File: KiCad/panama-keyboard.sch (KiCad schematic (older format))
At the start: 170 parts, among them J1 MX, J2 USB_C_Receptacle_USB2.0, J3 AVR-ISP-6, K1 MX, M1 MX, P1 MX, Q1 MX, T1 MX, U1 MX, U2 ATmega32A-PU, X1 MX, Y1 MX, Y2 Crystal

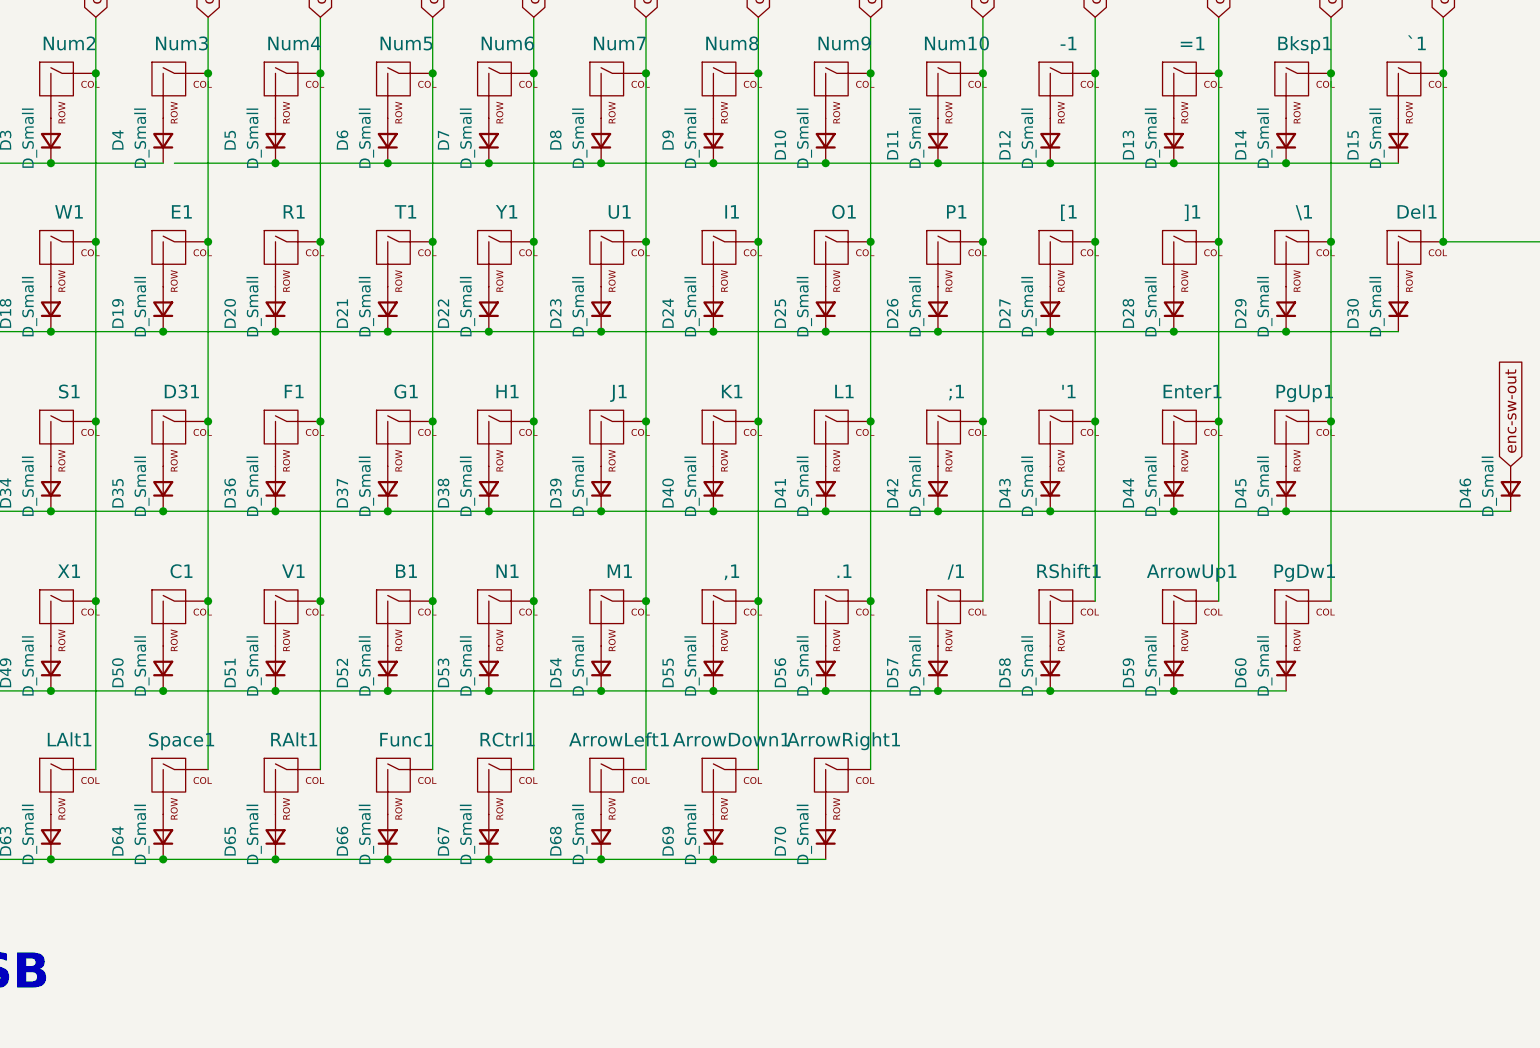
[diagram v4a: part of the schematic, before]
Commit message: pcb progress, moved switch matrix
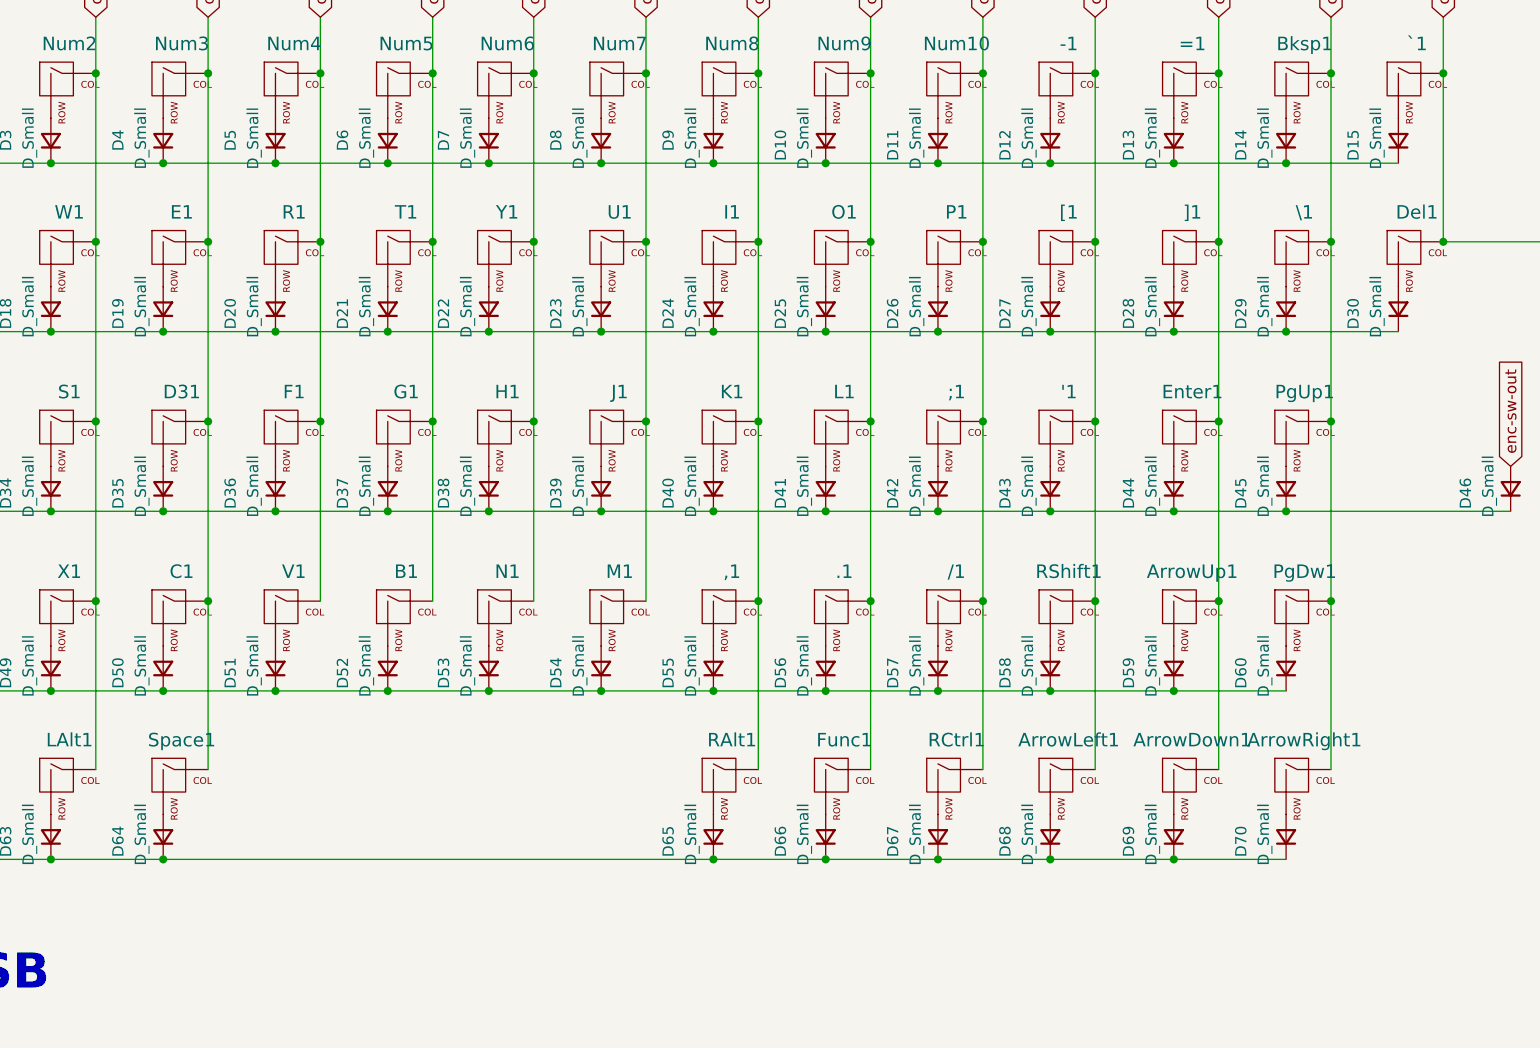
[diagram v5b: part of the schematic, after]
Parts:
- J3: footprint Connector_PinHeader_2.54mm:PinHeader_2x03_P2.54mm_Vertical -> Connector_PinHeader_2.54mm:PinHeader_1x06_P2.54mm_Horizontal
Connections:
- net col10: now also RCtrl1.1 (COL)
- net col11: now also ArrowLeft1.1 (COL)
- net col12: now also ArrowDown1.1 (COL)
- net col13: now also ArrowRight1.1 (COL)
- net col4: no longer RAlt1.1 (COL)
- net col5: no longer Func1.1 (COL)
- net col6: no longer RCtrl1.1 (COL)
- net col7: no longer ArrowLeft1.1 (COL)
- net col8: now also RAlt1.1 (COL); no longer ArrowDown1.1 (COL)
- net col9: now also Func1.1 (COL); no longer ArrowRight1.1 (COL)
- net row0: now also D10.1 (K), D11.1 (K), D12.1 (K), D13.1 (K), D14.1 (K), D15.1 (K), D5.1 (K), D6.1 (K), D7.1 (K), D8.1 (K), D9.1 (K)
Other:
- moved on the sheet: ArrowDown1, ArrowLeft1, ArrowRight1, D65, D66, D67, D68, D69, D70, Func1, RAlt1, RCtrl1
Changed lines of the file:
@@
 L Keyboard:MX RAlt1
 U 1 1 5F1DF75E
-P 6850 4600
-F 0 "RAlt1" H 6883 4781 60  0000 C CNN
-F 1 "MX" H 6825 4650 20  0001 C CNN
-F 2 "Button_Switch_Keyboard:SW_Cherry_MX_1.00u_PCB" H 6225 4575 60  0001 C CNN
-F 3 "" H 6225 4575 60  0001 C CNN
-	1    6850 4600
+P 8800 4600
+F 0 "RAlt1" H 8833 4781 60  0000 C CNN
+F 1 "MX" H 8775 4650 20  0001 C CNN
+F 2 "Button_Switch_Keyboard:SW_Cherry_MX_1.00u_PCB" H 8175 4575 60  0001 C CNN
+F 3 "" H 8175 4575 60  0001 C CNN
+	1    8800 4600
 	1    0    0    -1
 $EndComp
@@
 L Device:D_Small D65
 U 1 1 5F1DF76A
-P 6800 4850
-F 0 "D65" H 6850 5050 50  0000 R CNN
-F 1 "D_Small" H 6950 4950 50  0000 R CNN
-F 2 "Diode_THT:D_DO-35_SOD27_P7.62mm_Horizontal" V 6800 4850 50  0001 C CNN
-F 3 "~" V 6800 4850 50  0001 C CNN
-	1    6800 4850
-	0    -1   -1   0
-$EndComp
-$Comp
-L Keyboard:MX Func1
-U 1 1 5F1DF770
-P 7350 4600
-F 0 "Func1" H 7383 4781 60  0000 C CNN
-F 1 "MX" H 7325 4650 20  0001 C CNN
-F 2 "Button_Switch_Keyboard:SW_Cherry_MX_1.00u_PCB" H 6725 4575 60  0001 C CNN
-F 3 "" H 6725 4575 60  0001 C CNN
-	1    7350 4600
-	1    0    0    -1
-$EndComp
-$Comp
-L Device:D_Small D66
-U 1 1 5F1DF776
-P 7300 4850
-F 0 "D66" H 7350 5050 50  0000 R CNN
-F 1 "D_Small" H 7450 4950 50  0000 R CNN
-F 2 "Diode_THT:D_DO-35_SOD27_P7.62mm_Horizontal" V 7300 4850 50  0001 C CNN
-F 3 "~" V 7300 4850 50  0001 C CNN
-	1    7300 4850
-	0    -1   -1   0
-$EndComp
-$Comp
-L Keyboard:MX ArrowLeft1
-U 1 1 5F1DF77C
-P 8300 4600
-F 0 "ArrowLeft1" H 8333 4781 60  0000 C CNN
-F 1 "MX" H 8275 4650 20  0001 C CNN
-F 2 "Button_Switch_Keyboard:SW_Cherry_MX_1.00u_PCB" H 7675 4575 60  0001 C CNN
-F 3 "" H 7675 4575 60  0001 C CNN
-	1    8300 4600
-	1    0    0    -1
-$EndComp
-$Comp
-L Keyboard:MX ArrowDown1
-U 1 1 5F1DF782
-P 8800 4600
-F 0 "ArrowDown1" H 8833 4781 60  0000 C CNN
-F 1 "MX" H 8775 4650 20  0001 C CNN
-F 2 "Button_Switch_Keyboard:SW_Cherry_MX_1.00u_PCB" H 8175 4575 60  0001 C CNN
-F 3 "" H 8175 4575 60  0001 C CNN
-	1    8800 4600
-	1    0    0    -1
-$EndComp
-$Comp
-L Device:D_Small D68
-U 1 1 5F1DF788
-P 8250 4850
-F 0 "D68" H 8300 5050 50  0000 R CNN
-F 1 "D_Small" H 8400 4950 50  0000 R CNN
-F 2 "Diode_THT:D_DO-35_SOD27_P7.62mm_Horizontal" V 8250 4850 50  0001 C CNN
-F 3 "~" V 8250 4850 50  0001 C CNN
-	1    8250 4850
-	0    -1   -1   0
-$EndComp
-$Comp
-L Device:D_Small D69
-U 1 1 5F1DF78E
 P 8750 4850
-F 0 "D69" H 8800 5050 50  0000 R CNN
+F 0 "D65" H 8800 5050 50  0000 R CNN
 F 1 "D_Small" H 8900 4950 50  0000 R CNN
 F 2 "Diode_THT:D_DO-35_SOD27_P7.62mm_Horizontal" V 8750 4850 50  0001 C CNN
@@
 $EndComp
 $Comp
-L Keyboard:MX ArrowRight1
-U 1 1 5F1DF794
+L Keyboard:MX Func1
+U 1 1 5F1DF770
 P 9300 4600
-F 0 "ArrowRight1" H 9333 4781 60  0000 C CNN
+F 0 "Func1" H 9333 4781 60  0000 C CNN
 F 1 "MX" H 9275 4650 20  0001 C CNN
 F 2 "Button_Switch_Keyboard:SW_Cherry_MX_1.00u_PCB" H 8675 4575 60  0001 C CNN
@@
 $EndComp
 $Comp
-L Device:D_Small D70
-U 1 1 5F1DF79A
+L Device:D_Small D66
+U 1 1 5F1DF776
 P 9250 4850
-F 0 "D70" H 9300 5050 50  0000 R CNN
+F 0 "D66" H 9300 5050 50  0000 R CNN
 F 1 "D_Small" H 9400 4950 50  0000 R CNN
 F 2 "Diode_THT:D_DO-35_SOD27_P7.62mm_Horizontal" V 9250 4850 50  0001 C CNN
 F 3 "~" V 9250 4850 50  0001 C CNN
 	1    9250 4850
+	0    -1   -1   0
+$EndComp
+$Comp
+L Keyboard:MX ArrowLeft1
+U 1 1 5F1DF77C
+P 10300 4600
+F 0 "ArrowLeft1" H 10333 4781 60  0000 C CNN
+F 1 "MX" H 10275 4650 20  0001 C CNN
+F 2 "Button_Switch_Keyboard:SW_Cherry_MX_1.00u_PCB" H 9675 4575 60  0001 C CNN
+F 3 "" H 9675 4575 60  0001 C CNN
+	1    10300 4600
+	1    0    0    -1
+$EndComp
+$Comp
+L Keyboard:MX ArrowDown1
+U 1 1 5F1DF782
+P 10850 4600
+F 0 "ArrowDown1" H 10883 4781 60  0000 C CNN
+F 1 "MX" H 10825 4650 20  0001 C CNN
+F 2 "Button_Switch_Keyboard:SW_Cherry_MX_1.00u_PCB" H 10225 4575 60  0001 C CNN
+F 3 "" H 10225 4575 60  0001 C CNN
+	1    10850 4600
+	1    0    0    -1
+$EndComp
+$Comp
+L Device:D_Small D68
+U 1 1 5F1DF788
+P 10250 4850
+F 0 "D68" H 10300 5050 50  0000 R CNN
+F 1 "D_Small" H 10400 4950 50  0000 R CNN
+F 2 "Diode_THT:D_DO-35_SOD27_P7.62mm_Horizontal" V 10250 4850 50  0001 C CNN
+F 3 "~" V 10250 4850 50  0001 C CNN
+	1    10250 4850
+	0    -1   -1   0
+$EndComp
+$Comp
+L Device:D_Small D69
+U 1 1 5F1DF78E
+P 10800 4850
+F 0 "D69" H 10850 5050 50  0000 R CNN
+F 1 "D_Small" H 10950 4950 50  0000 R CNN
+F 2 "Diode_THT:D_DO-35_SOD27_P7.62mm_Horizontal" V 10800 4850 50  0001 C CNN
+F 3 "~" V 10800 4850 50  0001 C CNN
+	1    10800 4850
 	0    -1   -1   0
 $EndComp
@@
 	5800 1850 6300 1850
 Connection ~ 5800 1850
-Wire Wire Line
-	6350 1850 6800 1850
 Connection ~ 6800 1850
 Wire Wire Line
@@
 Wire Wire Line
 	5800 4950 6300 4950
-Connection ~ 6300 4950
-Wire Wire Line
-	6300 4950 6800 4950
-Connection ~ 6800 4950
-Connection ~ 8250 4950
-Wire Wire Line
-	8250 4950 8750 4950
 Connection ~ 8750 4950
-Wire Wire Line
-	8750 4950 9250 4950
 Wire Wire Line
 	5500 1200 5500 1450
@@
 Wire Wire Line
 	7000 3000 7000 3800
-Connection ~ 7000 3800
-Wire Wire Line
-	7000 3800 7000 4550
+Wire Wire Line
+	8950 3800 8950 4550
 Wire Wire Line
 	7500 1200 7500 1450
@@
 Wire Wire Line
 	7500 3000 7500 3800
-Connection ~ 7500 3800
-Wire Wire Line
-	7500 3800 7500 4550
+Wire Wire Line
+	9450 3800 9450 4550
 Wire Wire Line
 	7950 1200 7950 1450
@@
 	7950 3000 7950 3800
 Wire Wire Line
-	8450 3800 8450 4550
+	10450 3800 10450 4550
 Wire Wire Line
 	8450 1200 8450 1450
@@
 Wire Wire Line
 	8450 3000 8450 3800
-Connection ~ 8450 3800
-Wire Wire Line
-	8950 3800 8950 4550
+Wire Wire Line
+	11000 3800 11000 4550
 Wire Wire Line
 	8950 1200 8950 1450
@@
 Wire Wire Line
 	8950 3000 8950 3800
-Connection ~ 8950 3800
-Wire Wire Line
-	9450 3800 9450 4550
 Wire Wire Line
 	9450 1200 9450 1450
@@
 F 0 "J3" H 4771 9396 50  0000 R CNN
 F 1 "AVR-ISP-6" H 4771 9305 50  0000 R CNN
-F 2 "Connector_PinHeader_2.54mm:PinHeader_2x03_P2.54mm_Vertical" V 4850 9350 50  0001 C CNN
+F 2 "Connector_PinHeader_2.54mm:PinHeader_1x06_P2.54mm_Horizontal" V 4850 9350 50  0001 C CNN
 F 3 " ~" H 3825 8750 50  0001 C CNN
 	1    5100 9300
@@
 	1    0    0    -1
 $EndComp
-Connection ~ 9450 3800
-Wire Wire Line
-	6800 4950 7300 4950
+Wire Wire Line
+	8750 4950 9250 4950
 $Comp
 L Keyboard:MX RCtrl1
 U 1 1 5F24CC72
-P 7800 4600
-F 0 "RCtrl1" H 7833 4781 60  0000 C CNN
-F 1 "MX" H 7775 4650 20  0001 C CNN
-F 2 "Button_Switch_Keyboard:SW_Cherry_MX_1.00u_PCB" H 7175 4575 60  0001 C CNN
-F 3 "" H 7175 4575 60  0001 C CNN
-	1    7800 4600
+P 9800 4600
+F 0 "RCtrl1" H 9833 4781 60  0000 C CNN
+F 1 "MX" H 9775 4650 20  0001 C CNN
+F 2 "Button_Switch_Keyboard:SW_Cherry_MX_1.00u_PCB" H 9175 4575 60  0001 C CNN
+F 3 "" H 9175 4575 60  0001 C CNN
+	1    9800 4600
 	1    0    0    -1
 $EndComp
@@
 L Device:D_Small D67
 U 1 1 5F24CC78
-P 7750 4850
-F 0 "D67" H 7800 5050 50  0000 R CNN
-F 1 "D_Small" H 7900 4950 50  0000 R CNN
-F 2 "Diode_THT:D_DO-35_SOD27_P7.62mm_Horizontal" V 7750 4850 50  0001 C CNN
-F 3 "~" V 7750 4850 50  0001 C CNN
-	1    7750 4850
+P 9750 4850
+F 0 "D67" H 9800 5050 50  0000 R CNN
+F 1 "D_Small" H 9900 4950 50  0000 R CNN
+F 2 "Diode_THT:D_DO-35_SOD27_P7.62mm_Horizontal" V 9750 4850 50  0001 C CNN
+F 3 "~" V 9750 4850 50  0001 C CNN
+	1    9750 4850
 	0    -1   -1   0
 $EndComp
 Wire Wire Line
-	7950 3800 7950 4550
-Connection ~ 7950 3800
-Wire Wire Line
-	7750 4950 7300 4950
-Connection ~ 7300 4950
-Wire Wire Line
-	7750 4950 8250 4950
-Connection ~ 7750 4950
+	9950 3800 9950 4550
+Wire Wire Line
+	9750 4950 10250 4950
 $Comp
 L Keyboard:WS2811 D71
@@
 	10950 7000 11750 7000
 NoConn ~ 12050 7850
+Wire Wire Line
+	11500 3800 11500 4550
+Wire Wire Line
+	10800 4950 11300 4950
+$Comp
+L Device:D_Small D70
+U 1 1 5F1DF79A
+P 11300 4850
+F 0 "D70" H 11350 5050 50  0000 R CNN
+F 1 "D_Small" H 11450 4950 50  0000 R CNN
+F 2 "Diode_THT:D_DO-35_SOD27_P7.62mm_Horizontal" V 11300 4850 50  0001 C CNN
+F 3 "~" V 11300 4850 50  0001 C CNN
+	1    11300 4850
+	0    -1   -1   0
+$EndComp
+$Comp
+L Keyboard:MX ArrowRight1
+U 1 1 5F1DF794
+P 11350 4600
+F 0 "ArrowRight1" H 11383 4781 60  0000 C CNN
+F 1 "MX" H 11325 4650 20  0001 C CNN
+F 2 "Button_Switch_Keyboard:SW_Cherry_MX_1.00u_PCB" H 10725 4575 60  0001 C CNN
+F 3 "" H 10725 4575 60  0001 C CNN
+	1    11350 4600
+	1    0    0    -1
+$EndComp
+Connection ~ 11500 3800
+Connection ~ 10800 4950
+Connection ~ 11000 3800
+Connection ~ 10450 3800
+Wire Wire Line
+	10250 4950 10800 4950
+Connection ~ 10250 4950
+Connection ~ 9750 4950
+Connection ~ 9950 3800
+Connection ~ 8950 3800
+Connection ~ 9450 3800
+Wire Wire Line
+	6300 4950 8750 4950
+Connection ~ 6300 4950
+Wire Wire Line
+	9250 4950 9750 4950
+Connection ~ 9250 4950
+Wire Wire Line
+	6300 1850 6800 1850
+Connection ~ 6300 1850
 $EndSCHEMATC
